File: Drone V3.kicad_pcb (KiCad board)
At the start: 4 copper layers, 55 x 42 mm, 86 parts, among them J2 Phase Outputs, J3 Pad Terminals, J4 Signal, U1 IRS21867S, U13 STM32F303CBTx, U4 INA180A3, U6 IRS21867S, U7 IRS21867S, U9 INA180A3

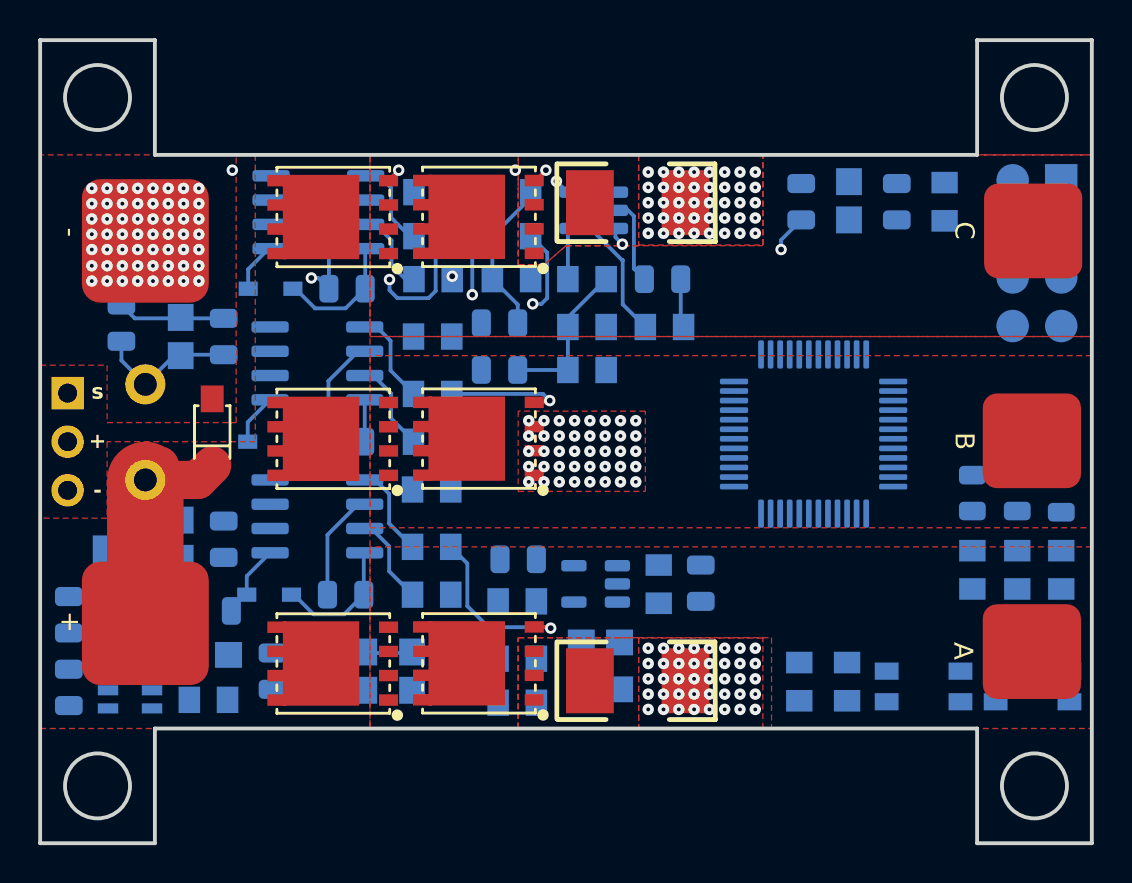
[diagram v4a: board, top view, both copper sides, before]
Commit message: Done with routing, partial review complete.
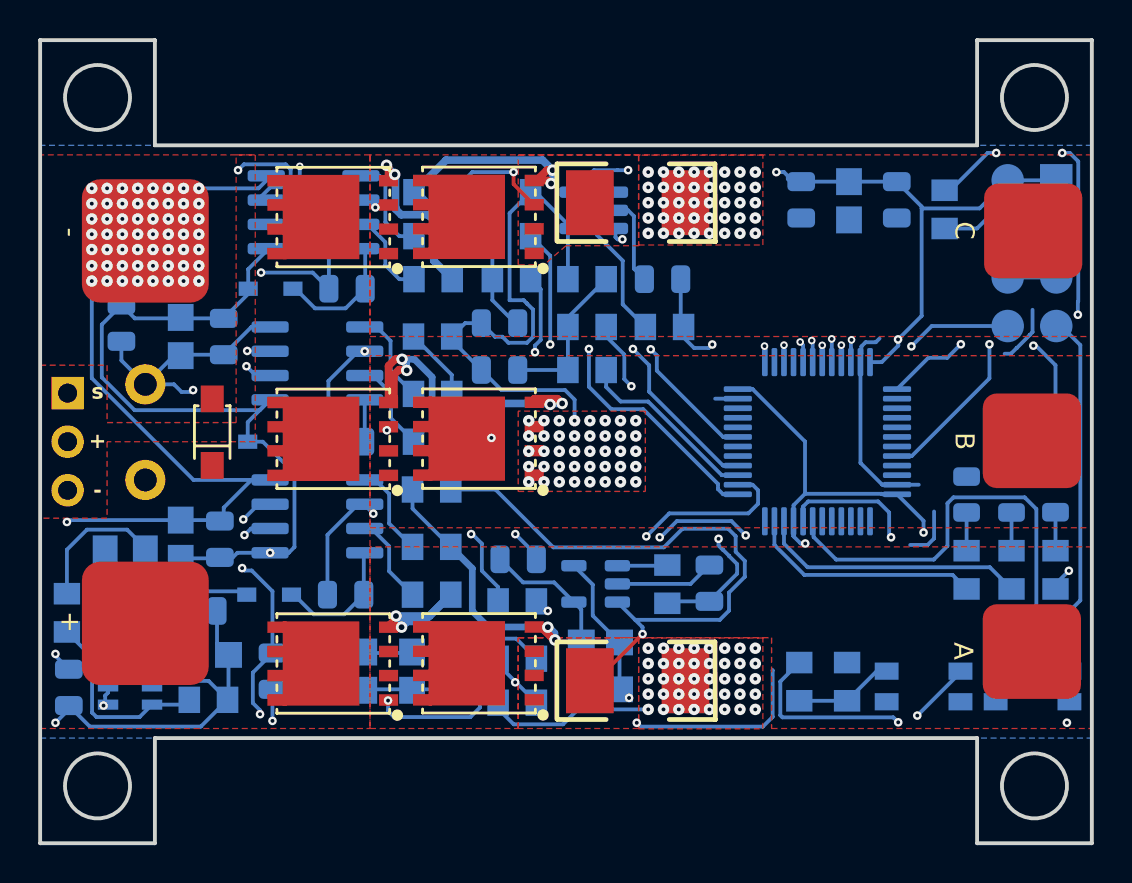
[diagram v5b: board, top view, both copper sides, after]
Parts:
- moved C36 5.00 mm to (61.3, 124.8), turned to -90 degrees
- moved C38 5.00 mm to (66.3, 124.8), turned to -90 degrees
- moved R39 3.41 mm to (22.9, 146.4), turned to -90 degrees
- moved C43 3.29 mm to (26.2, 147.1), turned to 0 degrees
- moved C23 0.75 mm to (29.8, 146.3)
- moved C40 0.45 mm to (56.5, 144.9)
- moved R29 0.45 mm to (54.3, 144.9)
- moved U13 0.45 mm to (62.1, 137.5), turned to 90 degrees
- moved R34 0.40 mm to (68.8, 125.3)
- moved D14 0.31 mm to (72.3, 140.3)
- moved D15 0.31 mm to (70.0, 140.3)
- moved D17 0.30 mm to (74.6, 140.2)
- moved R35 0.30 mm to (74.6, 144.2)
- moved R32 0.30 mm to (72.3, 144.2)
- moved R33 0.30 mm to (70.0, 144.2)
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- renumbered BOOT0_SW1 to B0, NRST_SW1 to RST
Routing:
- net /ESC1/+3V3MCU: track 26.3 -> 161.1 mm, vias 2 -> 9
- net /ESC1/-ESC: track 10.2 -> 137.9 mm, vias 176 -> 180
- net /ESC1/-3V3MCU: track 0.07 -> 102.4 mm, vias 0 -> 4
- net /ESC1/+12V: track 13.7 -> 111.9 mm, vias 0 -> 2
- net /ESC1/MCU_CH: track 0.00 -> 68.1 mm, vias 0 -> 2
- net /ESC1/SIG_ESC: track 0.00 -> 64.7 mm, vias 0 -> 1
- net /ESC1/MCU_AL: track 0.00 -> 59.9 mm, vias 0 -> 2
- net Net-(U13-PA3): track 0.00 -> 52.4 mm, vias 0 -> 2
- net Net-(U13-BOOT0): track 0.00 -> 51.7 mm, vias 0 -> 2
- net /ESC1/MCU_BL: track 0.00 -> 45.2 mm, vias 0 -> 2
- net /ESC1/MCU_AH: track 0.00 -> 42.9 mm, vias 0 -> 4
- net /ESC1/NRST: track 0.00 -> 42.2 mm
- net /ESC1/MCU_CL: track 0.00 -> 38.2 mm, vias 0 -> 2
- net /ESC1/MCU_BH: track 0.00 -> 35.8 mm, vias 0 -> 2
- net /ESC1/Shunt_A: track 0.00 -> 32.2 mm, vias 0 -> 1
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- added copper zone on B.Cu, net /ESC1/-3V3MCU
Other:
- outline, holes or cut-outs redrawn

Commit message: Final draft
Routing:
- net /ESC1/B_Phase: track 23.9 -> 23.3 mm
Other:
- board text added: "Fagan '27"

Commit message: ESC PCB Finalized Iteration #1
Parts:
- added ?: , , F.Cu at (23.0, 143.1)
- added ?: , , F.Cu at (33.6, 147.2)
- added G***: LOGO, LOGO, B.Cu at (67.6, 129.7)
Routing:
- net /ESC1/MCU_BL: track 45.2 -> 45.8 mm
- net /ESC1/MCU_BH: track 35.8 -> 36.4 mm
- net /ESC1/MCU_CFB: track 19.0 -> 19.6 mm
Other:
- outline, holes or cut-outs redrawn
- board text added: "Fagan"
- board text removed: "Fagan '27"
